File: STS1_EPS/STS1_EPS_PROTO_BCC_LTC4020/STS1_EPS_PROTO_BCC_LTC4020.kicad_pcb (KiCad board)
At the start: 2 copper layers, 85 x 85 mm, 98 parts, among them CON1 DISCO-CON1, CON11 DISCO-CON1, CON2 DISCO-CON2, CON21 DISCO-CON2, J1 1729267, J10 BG2, J11 BGATE, J2 Output, J3 Terminal BAT, J4 External NTC, J5 VIN_REG, J6 SHDN, J7 TG1, J8 TG2, J9 BG1, Q1 SI7135DP-T1-GE3, U1 LTC4020EUHF-PBF, U2 SI7272DP-T1-GE3, U3 SI7272DP-T1-GE3, U4 coordinate_system, U5 logo

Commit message: BCC ready for review
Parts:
- removed U5: logo, footprints:STLogoTiny
- moved D4 101.7 mm to (117.8, 117.0), turned to 180 degrees
- moved D1 96.0 mm to (117.8, 112.9), turned to 180 degrees
- moved R5 40.8 mm to (121.5, 117.0), turned to 0 degrees
- moved R3 36.9 mm to (121.5, 112.9), turned to 0 degrees
- moved R20 15.5 mm to (137.5, 64.2)
- moved JP17 14.4 mm to (137.8, 68.2)
- moved C2 14.3 mm to (131.7, 68.0)
- moved C1 14.3 mm to (131.4, 63.6)
- moved J2 14.2 mm to (132.9, 55.5)
- moved J11 5.24 mm to (126.6, 74.6)
- moved JP14 5.23 mm to (184.0, 73.5), turned to 90 degrees
- moved C8 3.31 mm to (131.2, 75.1)
- moved R15 3.31 mm to (131.2, 78.4)
- moved R17 3.31 mm to (131.2, 71.8)
- moved JP20 2.63 mm to (136.7, 77.6)
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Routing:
- net /EPS Battery Charger/VFBMAX: track 0.00 -> 64.9 mm, vias 0 -> 5
- net /EPS Battery Charger/SHDN: track 10.6 -> 69.0 mm, vias 0 -> 2
- net /EPS Battery Charger/SENSBOT: track 5.19 -> 56.0 mm, vias 0 -> 3
- net /EPS Battery Charger/CSP: track 8.88 -> 57.0 mm, vias 0 -> 4
- net GND: track 36.6 -> 84.8 mm, vias 115 -> 121
- net /EPS Battery Charger/ITH: track 0.00 -> 46.0 mm, vias 0 -> 4
- net /EPS Battery Charger/FAULT: track 5.25 -> 50.1 mm, vias 0 -> 4
- net /EPS Battery Charger/CHARGING: track 5.42 -> 47.9 mm, vias 0 -> 4
- net /EPS Battery Charger/SENSVIN: track 4.33 -> 33.7 mm, vias 0 -> 3
- net /EPS Battery Charger/ILIMIT: track 0.00 -> 28.9 mm, vias 0 -> 5
- net /EPS Battery Charger/VIN_REG: track 9.85 -> 38.3 mm, vias 0 -> 1
- net /EPS Battery Charger/SENSTOP: track 7.14 -> 31.7 mm, vias 0 -> 3
- net Net-(JP20-Pad2): track 35.3 -> 47.5 mm, vias 2 -> 1
- net Net-(C1-Pad1): track 10.3 -> 0.00 mm
- net /EPS Battery Charger/SW1: track 44.1 -> 51.1 mm, vias 6 -> 2
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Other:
- board text added: "Charge"
- board text removed: "Charging"

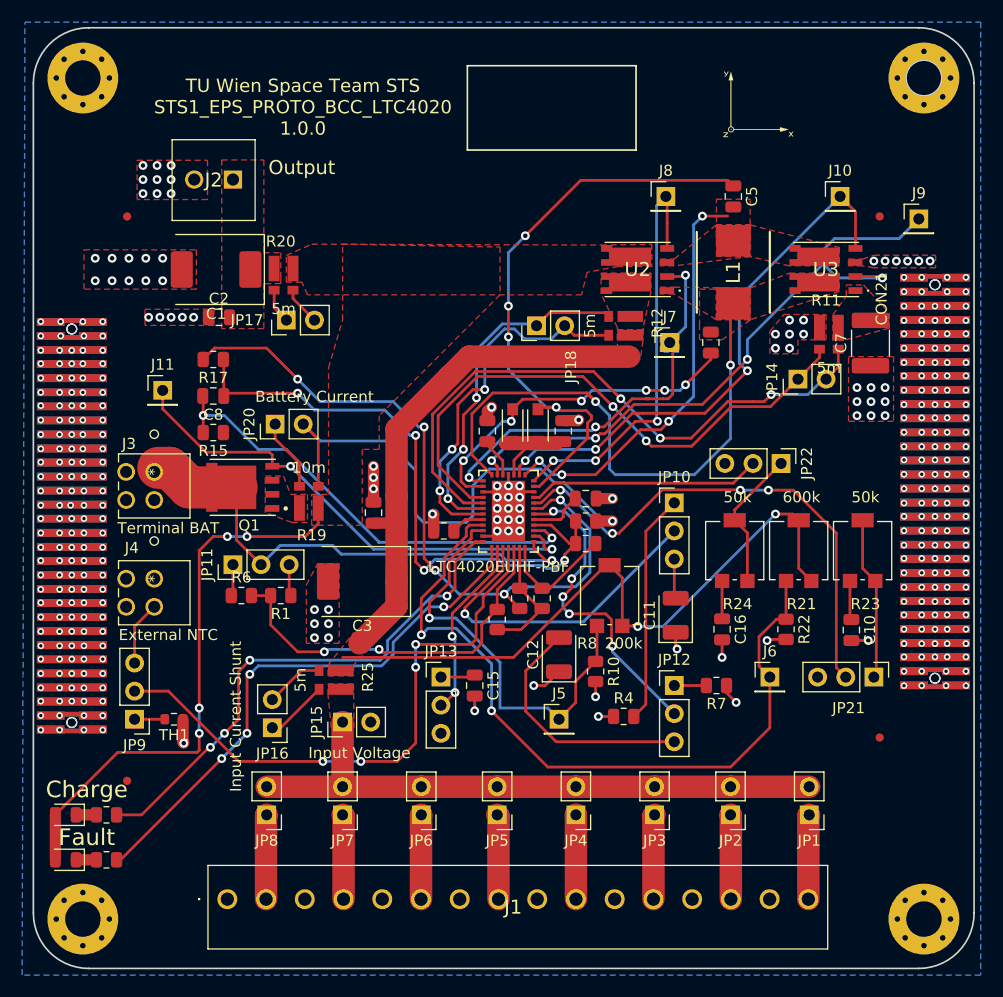
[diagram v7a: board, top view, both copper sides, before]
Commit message: Incorporated feedback into BCC and SCC - Fixed "unspecified" pin type warnings - Added correct test point symbols - Added thermal blockers - Added DRC parameters and fixed DRC issues - Adapted CubeSat STS1 PCB template to not violate DRC
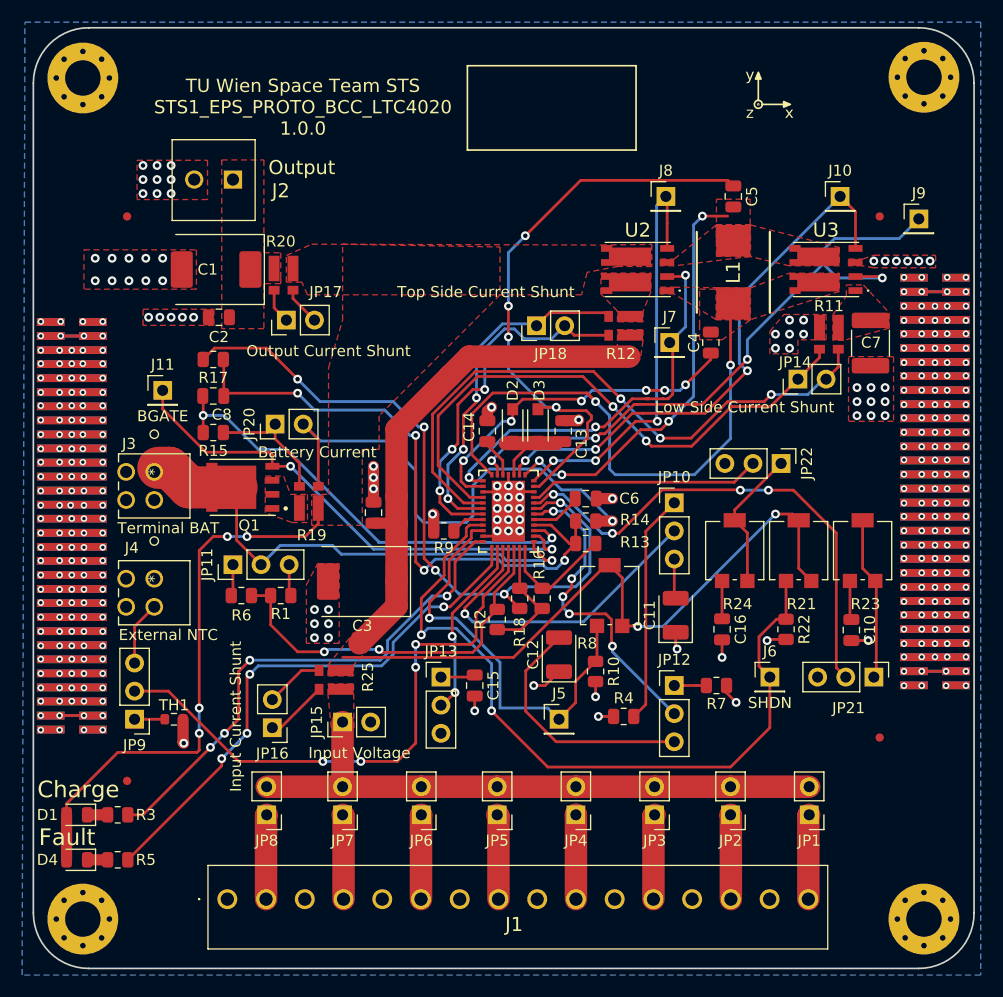
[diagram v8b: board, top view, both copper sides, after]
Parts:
- removed REF**: MountingHole_3.2mm_M3, Mounting_Holes:MountingHole_3.2mm_M3
- moved D1 1.02 mm to (118.8, 112.9)
- moved D4 1.02 mm to (118.8, 117.0)
- moved R3 1.02 mm to (122.5, 112.9)
- moved R5 1.02 mm to (122.5, 117.0)
- moved H2 0.07 mm to (195.4, 46.3)
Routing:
- net Net-(CON2-Pad2): track 0.00 -> 7.62 mm
- net Net-(CON1-Pad29): track 0.00 -> 7.62 mm
- net Net-(CON1-Pad2): track 0.00 -> 7.62 mm
- net GND: track 84.8 -> 92.4 mm
- net Net-(JP20-Pad1): track 6.54 -> 11.5 mm
- net /EPS Battery Charger/CHARGING: track 47.9 -> 47.0 mm
- removed copper zone on B.Cu, net /EPS Battery Charger/TG1
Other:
- net class Default: clearance 0.2 -> 0.15; trace_width 0.25 -> 0.254
- rule trace_clearance: 0.2 -> 0.15
- rule trace_min: 0.2 -> 0.15
- rule via_min_size: 0.4 -> 0.3
